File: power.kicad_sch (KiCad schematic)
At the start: 18 parts, among them IC1 STM32MP157AAB3

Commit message: Added Symbols
- MCP73830T
- STPMIC1BPQR
- MT41K256M16TW
- MCP73830
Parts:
- removed IC?: STPMIC1EPQR, QFN40P500X600X80-45N-D, symbol mp1lib:STPMIC1EPQR
- added IC2: STPMIC1BPQR, QFN40P500X600X80-45N-D, symbol ARMband:STPMIC1BPQR
- added IC3: STC3117IJT, BGA9C40P3X3_146X156X66, symbol ARMband:STC3117IJT
- added IC4: MCP73830T-2AAI_MYY, SON50P200X200X80-7N-D, symbol ARMband:MCP73830T-2AAI_MYY
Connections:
- net BUCK1IN: now also IC2.12 (BUCK2IN), IC2.24 (BUCK4IN), IC2.28 (BUCK3IN), IC2.8 (BUCK1IN)
- net BUCK_1V2: now also IC2.5 (VOUT1)
- net BUCK_1V8: now also IC2.31 (VOUT3)
- net BUCK_3V3: now also IC2.27 (VOUT4)
- net GND: now also IC2.10 (PGND2), IC2.26 (PGND4), IC2.30 (PGND3), IC2.6 (PGND1)
- net LDO1_1V8: now also IC2.23 (LDO1OUT)
- net VDD_DDR: now also IC2.9 (VOUT2)
- net VLX1: now also IC2.7 (VLX1)
- net VLX2: now also IC2.11 (VLX2)
- net VLX3: now also IC2.29 (VLX3)
- net VLX4: now also IC2.25 (VLX4)
- net VREF_DDR: now also IC2.16 (VREFDDR)
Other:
- note removed: "TODO: remake symbol + add to library! ;("
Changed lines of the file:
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@@
     (effects (font (size 1.27 1.27)) (justify left bottom))
-  )
-  (text "TODO: remake symbol + add to library! ;(" (at 57.15 123.19 0)
-    (effects (font (face "Yu Gothic UI") (size 2.54 2.54) (thickness 0.508) bold (color 255 0 6 1)) (justify left bottom))
   )
   (text "A:\n3V3 500mA @ HP mode\n	50 - 200 mA @ LP mode\nB:\n1V8 500mA @ HP mode\n	50 - 200 mA @ LP mode"
@@
         (path "/017c50c6-333c-4d31-ad5a-278994a09b14/5731d22b-18c2-4920-9f80-2a6ce209edf2"
           (reference "#PWR?") (unit 1)
+        )
+      )
+    )
+  )
+  (symbol (lib_id "ARMband:STPMIC1BPQR") (at 67.31 49.53 0) (unit 1)
+    (in_bom yes) (on_board yes) (dnp no) (fields_autoplaced)
+    (property "Reference" "IC2" (at 99.7459 94.3817 0)
+      (effects (font (size 1.27 1.27)) (justify left))
+    )
+    (property "Value" "STPMIC1BPQR" (at 99.7459 96.3027 0)
+      (effects (font (size 1.27 1.27)) (justify left))
+    )
+    (property "Footprint" "QFN40P500X600X80-45N-D" (at 104.14 34.29 0)
+      (effects (font (size 1.27 1.27)) (justify left) hide)
+    )
+    (property "Datasheet" "" (at 104.14 36.83 0)
+      (effects (font (size 1.27 1.27)) (justify left) hide)
+    )
+    (property "Description" "Power Management Specialized - PMIC" (at 104.14 39.37 0)
+      (effects (font (size 1.27 1.27)) (justify left) hide)
+    )
+    (property "Height" "0.8" (at 104.14 41.91 0)
+      (effects (font (size 1.27 1.27)) (justify left) hide)
+    )
+    (property "Mouser Part Number" "511-STPMIC1BPQR" (at 104.14 44.45 0)
+      (effects (font (size 1.27 1.27)) (justify left) hide)
+    )
+    (property "Mouser Price/Stock" "https://www.mouser.co.uk/ProductDetail/STMicroelectronics/STPMIC1BPQR?qs=%252B6g0mu59x7I4ukJ6TbOLhg%3D%3D" (at 104.14 46.99 0)
+      (effects (font (size 1.27 1.27)) (justify left) hide)
+    )
+    (property "Manufacturer_Name" "STMicroelectronics" (at 104.14 49.53 0)
+      (effects (font (size 1.27 1.27)) (justify left) hide)
+    )
+    (property "Manufacturer_Part_Number" "STPMIC1BPQR" (at 104.14 52.07 0)
+      (effects (font (size 1.27 1.27)) (justify left) hide)
+    )
+    (pin "1")
+    (pin "10")
+    (pin "11")
+    (pin "12")
+    (pin "13")
+    (pin "14")
+    (pin "15")
+    (pin "16")
+    (pin "17")
+    (pin "18")
+    (pin "19")
+    (pin "2")
+    (pin "20")
+    (pin "21")
+    (pin "22")
+    (pin "23")
+    (pin "24")
+    (pin "25")
+    (pin "26")
+    (pin "27")
+    (pin "28")
+    (pin "29")
+    (pin "3")
+    (pin "30")
+    (pin "31")
+    (pin "32")
+    (pin "33")
+    (pin "34")
+    (pin "35")
+    (pin "36")
+    (pin "37")
+    (pin "38")
+    (pin "39")
+    (pin "4")
+    (pin "40")
+    (pin "41")
+    (pin "42")
+    (pin "43")
+    (pin "44")
+    (pin "45")
+    (pin "5")
+    (pin "6")
+    (pin "7")
+    (pin "8")
+    (pin "9")
+    (instances
+      (project "gba"
+        (path "/017c50c6-333c-4d31-ad5a-278994a09b14/5731d22b-18c2-4920-9f80-2a6ce209edf2"
+          (reference "IC2") (unit 1)
         )
       )
@@
     )
   )
+  (symbol (lib_id "ARMband:STC3117IJT") (at 25.4 120.65 0) (unit 1)
+    (in_bom yes) (on_board yes) (dnp no) (fields_autoplaced)
+    (property "Reference" "IC3" (at 39.37 115.1509 0)
+      (effects (font (size 1.27 1.27)))
+    )
+    (property "Value" "STC3117IJT" (at 39.37 117.0719 0)
+      (effects (font (size 1.27 1.27)))
+    )
+    (property "Footprint" "BGA9C40P3X3_146X156X66" (at 49.53 118.11 0)
+      (effects (font (size 1.27 1.27)) (justify left) hide)
+    )
+    (property "Datasheet" "http://www.st.com/content/ccc/resource/technical/document/datasheet/ea/b5/01/6e/dd/f0/49/3e/DM00105047.pdf/files/DM00105047.pdf/jcr:content/translations/en.DM00105047.pdf" (at 49.53 120.65 0)
+      (effects (font (size 1.27 1.27)) (justify left) hide)
+    )
+    (property "Description" "Battery Management ANALOG" (at 49.53 123.19 0)
+      (effects (font (size 1.27 1.27)) (justify left) hide)
+    )
+    (property "Height" "0.655" (at 49.53 125.73 0)
+      (effects (font (size 1.27 1.27)) (justify left) hide)
+    )
+    (property "Mouser Part Number" "511-STC3117IJT" (at 49.53 128.27 0)
+      (effects (font (size 1.27 1.27)) (justify left) hide)
+    )
+    (property "Mouser Price/Stock" "https://www.mouser.co.uk/ProductDetail/STMicroelectronics/STC3117IJT?qs=JkuGhO7zlpmFAm2OGW2bCw%3D%3D" (at 49.53 130.81 0)
+      (effects (font (size 1.27 1.27)) (justify left) hide)
+    )
+    (property "Manufacturer_Name" "STMicroelectronics" (at 49.53 133.35 0)
+      (effects (font (size 1.27 1.27)) (justify left) hide)
+    )
+    (property "Manufacturer_Part_Number" "STC3117IJT" (at 49.53 135.89 0)
+      (effects (font (size 1.27 1.27)) (justify left) hide)
+    )
+    (pin "A1")
+    (pin "A2")
+    (pin "A3")
+    (pin "B1")
+    (pin "B2")
+    (pin "B3")
+    (pin "C1")
+    (pin "C2")
+    (pin "C3")
+    (instances
+      (project "gba"
+        (path "/017c50c6-333c-4d31-ad5a-278994a09b14/5731d22b-18c2-4920-9f80-2a6ce209edf2"
+          (reference "IC3") (unit 1)
+        )
+      )
+    )
+  )
   (symbol (lib_id "Device:L_Small") (at 238.76 52.07 90) (unit 1)
     (in_bom yes) (on_board yes) (dnp no) (fields_autoplaced)
@@
         (path "/017c50c6-333c-4d31-ad5a-278994a09b14/5731d22b-18c2-4920-9f80-2a6ce209edf2"
           (reference "#PWR?") (unit 1)
-        )
-      )
-    )
-  )
-  (symbol (lib_id "mp1lib:STPMIC1EPQR") (at 67.31 49.53 0) (unit 1)
-    (in_bom yes) (on_board yes) (dnp no) (fields_autoplaced)
-    (property "Reference" "IC?" (at 99.8094 94.8087 0)
-      (effects (font (size 1.27 1.27)) (justify left))
-    )
-    (property "Value" "STPMIC1EPQR" (at 99.8094 97.5838 0)
-      (effects (font (size 1.27 1.27)) (justify left))
-    )
-    (property "Footprint" "QFN40P500X600X80-45N-D" (at 104.14 34.29 0)
-      (effects (font (size 1.27 1.27)) (justify left) hide)
-    )
-    (property "Datasheet" "https://www.arrow.com/en/products/stpmic1epqr/stmicroelectronics" (at 104.14 36.83 0)
-      (effects (font (size 1.27 1.27)) (justify left) hide)
-    )
-    (property "Description" "Power Management Specialised - PMIC 14 Output Rails PMIC 4 Adjustable (COT) Buck SMPS converters BOOST with Bypass" (at 104.14 39.37 0)
-      (effects (font (size 1.27 1.27)) (justify left) hide)
-    )
-    (property "Height" "0.8" (at 104.14 41.91 0)
-      (effects (font (size 1.27 1.27)) (justify left) hide)
-    )
-    (property "Mouser Part Number" "511-STPMIC1EPQR" (at 104.14 44.45 0)
-      (effects (font (size 1.27 1.27)) (justify left) hide)
-    )
-    (property "Mouser Price/Stock" "https://www.mouser.co.uk/ProductDetail/STMicroelectronics/STPMIC1EPQR?qs=DPoM0jnrROUEouVjetqkFQ%3D%3D" (at 104.14 46.99 0)
-      (effects (font (size 1.27 1.27)) (justify left) hide)
-    )
-    (property "Manufacturer_Name" "STMicroelectronics" (at 104.14 49.53 0)
-      (effects (font (size 1.27 1.27)) (justify left) hide)
-    )
-    (property "Manufacturer_Part_Number" "STPMIC1EPQR" (at 104.14 52.07 0)
-      (effects (font (size 1.27 1.27)) (justify left) hide)
-    )
-    (pin "1")
-    (pin "10")
-    (pin "11")
-    (pin "12")
-    (pin "13")
-    (pin "14")
-    (pin "15")
-    (pin "16")
-    (pin "17")
-    (pin "18")
-    (pin "19")
-    (pin "2")
-    (pin "20")
-    (pin "21")
-    (pin "22")
-    (pin "23")
-    (pin "24")
-    (pin "25")
-    (pin "26")
-    (pin "27")
-    (pin "28")
-    (pin "29")
-    (pin "3")
-    (pin "30")
-    (pin "31")
-    (pin "32")
-    (pin "33")
-    (pin "34")
-    (pin "35")
-    (pin "36")
-    (pin "37")
-    (pin "38")
-    (pin "39")
-    (pin "4")
-    (pin "40")
-    (pin "41")
-    (pin "42")
-    (pin "43")
-    (pin "44")
-    (pin "45")
-    (pin "5")
-    (pin "6")
-    (pin "7")
-    (pin "8")
-    (pin "9")
-    (instances
-      (project "gba"
-        (path "/017c50c6-333c-4d31-ad5a-278994a09b14/5731d22b-18c2-4920-9f80-2a6ce209edf2"
-          (reference "IC?") (unit 1)
         )
       )
@@
         )
       )
+    )
+  )
+  (symbol (lib_id "ARMband:MCP73830T-2AAI_MYY") (at 24.13 151.13 0) (unit 1)
+    (in_bom yes) (on_board yes) (dnp no) (fields_autoplaced)
+    (property "Reference" "IC4" (at 39.37 145.6309 0)
+      (effects (font (size 1.27 1.27)))
+    )
+    (property "Value" "MCP73830T-2AAI_MYY" (at 39.37 147.5519 0)
+      (effects (font (size 1.27 1.27)))
+    )
+    (property "Footprint" "SON50P200X200X80-7N-D" (at 50.8 148.59 0)
+      (effects (font (size 1.27 1.27)) (justify left) hide)
+    )
+    (property "Datasheet" "http://www.microchip.com/mymicrochip/filehandler.aspx?ddocname=en555820" (at 50.8 151.13 0)
+      (effects (font (size 1.27 1.27)) (justify left) hide)
+    )
+    (property "Description" "Battery Management 1A LI-ION BATTERY CHARGE MGNT CNTRLR" (at 50.8 153.67 0)
+      (effects (font (size 1.27 1.27)) (justify left) hide)
+    )
+    (property "Height" "0.8" (at 50.8 156.21 0)
+      (effects (font (size 1.27 1.27)) (justify left) hide)
+    )
+    (property "Mouser Part Number" "579-MCP73830T2AAIMYY" (at 50.8 158.75 0)
+      (effects (font (size 1.27 1.27)) (justify left) hide)
+    )
+    (property "Mouser Price/Stock" "https://www.mouser.co.uk/ProductDetail/Microchip-Technology-Atmel/MCP73830T-2AAI-MYY?qs=DfG0HhEx1UUEr%2FUp7R8jlw%3D%3D" (at 50.8 161.29 0)
+      (effects (font (size 1.27 1.27)) (justify left) hide)
+    )
+    (property "Manufacturer_Name" "Microchip" (at 50.8 163.83 0)
+      (effects (font (size 1.27 1.27)) (justify left) hide)
+    )
+    (property "Manufacturer_Part_Number" "MCP73830T-2AAI/MYY" (at 50.8 166.37 0)
+      (effects (font (size 1.27 1.27)) (justify left) hide)
+    )
+    (pin "1")
+    (pin "2")
+    (pin "3")
+    (pin "4")
+    (pin "5")
+    (pin "6")
+    (pin "7")
+    (instances
+      (project "gba"
+        (path "/017c50c6-333c-4d31-ad5a-278994a09b14/5731d22b-18c2-4920-9f80-2a6ce209edf2"
+          (reference "IC4") (unit 1)
+        )
+      )

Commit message: Updated Symbols + Added Supply connections
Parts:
- removed C? (x4): 22uF, symbol Device:C_Small
- removed C? (x4): 10uF, symbol Device:C_Small
- removed IC2: STPMIC1BPQR, QFN40P500X600X80-45N-D, symbol ARMband:STPMIC1BPQR
- removed L? (x4): 1uH, symbol Device:L_Small
- removed R? (x4): 0R, symbol Device:R_Small
- added C10, C11, C12, C13, C14, C15, C16, C17, C18, C19, C20, C21, C22, C23, C24, C25, C26, C3, C4, C5, C6, C7, C8, C9: C_Small, symbol Device:C_Small
- added IC5: MT41K256M16TW-107_P, ARMband:BGA96C80P9X16_800X1400X120, symbol ARMband:MT41K256M16TW-107_P
- added IC6: STPMIC1BPQR, ARMband:QFN40P500X600X80-45N-D, symbol ARMband:STPMIC1BPQR
- added L1, L2, L3, L4, L5: L_Small, symbol Device:L_Small
- added R6, R7: R_Small, symbol Device:R_Small
- IC3: footprint BGA9C40P3X3_146X156X66 -> ARMband:BGA9C40P3X3_146X156X66
- IC4: footprint SON50P200X200X80-7N-D -> ARMband:SON50P200X200X80-7N-D
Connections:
- net BUCK_1V2: now also C7.2, IC6.5 (VOUT1), L1.2
- net BUCK_1V8: now also C9.2, IC6.31 (VOUT3), L3.2
- net BUCK_3V3: now also C10.2, IC6.27 (VOUT4), IC6.42 (VIO), L4.2, R6.1, R7.2; no longer IC1.W12 (VDD3V3_USBHS), IC1.W15 (VDD3V3_USBFS)
- net GND: now also IC3.A3 (GND), IC4.1 (VSS), IC4.7 (EP), C10.1, C11.1, C12.1, C13.1, C14.1, C15.1, C16.1, C17.1, C18.1, C19.1, C20.1, C21.1, C22.1, C23.1, C24.1, C25.1, C26.1, C3.1, C4.1, C5.1, C6.1, C7.1, C8.1, C9.1, IC5.A9 (VSS_1), IC5.B1 (VSSQ_1), IC5.B3 (VSS_2), IC5.B9 (VSSQ_2), IC5.D1 (VSSQ_3), IC5.D8 (VSSQ_4), IC5.E1 (VSS_3), IC5.E2 (VSSQ_5), IC5.E8 (VSSQ_6), IC5.F9 (VSSQ_7), IC5.G1 (VSSQ_8), IC5.G8 (VSS_4), IC5.G9 (VSSQ_9), IC5.J2 (VSS_5), IC5.J8 (VSS_6), IC5.M1 (VSS_7), IC5.M9 (VSS_8), IC5.P1 (VSS_9), IC5.P9 (VSS_10), IC5.T1 (VSS_11), IC5.T9 (VSS_12), IC6.10 (PGND2), IC6.15 (GNDLDO), IC6.26 (PGND4), IC6.30 (PGND3), IC6.41 (AGND), IC6.45 (EPGND), IC6.6 (PGND1)
- net VDD_DDR: now also C24.2, C8.2, IC5.A1 (VDDQ_1), IC5.A8 (VDDQ_2), IC5.B2 (VDD_1), IC5.C1 (VDDQ_3), IC5.C9 (VDDQ_4), IC5.D2 (VDDQ_5), IC5.D9 (VDD_2), IC5.E9 (VDDQ_6), IC5.F1 (VDDQ_7), IC5.G7 (VDD_3), IC5.H2 (VDDQ_8), IC5.H9 (VDDQ_9), IC5.K2 (VDD_4), IC5.K8 (VDD_5), IC5.N1 (VDD_6), IC5.N9 (VDD_7), IC5.R1 (VDD_8), IC5.R9 (VDD_9), IC6.13 (LDO3IN), IC6.9 (VOUT2), L2.2
- net VREF_DDR: now also C17.2, IC5.H1 (VREFDQ), IC5.M8 (VREFCA), IC6.16 (VREFDDR)
- new net: IC6.29 (VLX3), L3.1
- new net: IC6.11 (VLX2), L2.1
- new net: C15.2, IC6.40 (INTLDO)
- new net: IC6.33 (VLXBST), L5.2
- new net: IC6.25 (VLX4), L4.1
- new net: IC6.3 (SDA), R7.1
- new net: IC6.4 (SCL), R6.2
- new net: IC6.7 (VLX1), L1.1
- new net BSTOUT: C11.2, IC6.34 (BOUT), IC6.37 (SWIN)
- new net VBUS_HOST: C13.2, IC6.38 (SWOUT)
- new net VBUS_OTG: C12.2, IC6.35 (VBUSOTG)
- new net VDD_USB: C14.2, IC1.W12 (VDD3V3_USBHS), IC1.W15 (VDD3V3_USBFS), IC6.39 (LDO4OUT)
- new net VIN: C22.2, C23.2, C25.2, C26.2, C3.2, C4.2, C5.2, C6.2, IC6.12 (BUCK2IN), IC6.19 (LDO25IN), IC6.22 (LDO16IN), IC6.24 (BUCK4IN), IC6.28 (BUCK3IN), IC6.36 (VIN), IC6.8 (BUCK1IN), L5.1
- new net VOUT_LDO1: C18.2, IC6.23 (LDO1OUT)
- new net VOUT_LDO2: C20.2, IC6.18 (LDO2OUT)
- new net VOUT_LDO5: C21.2, IC6.20 (LDO5OUT)
- new net VOUT_LDO6: C19.2, IC6.21 (LDO6OUT)
- new net VOUT_LOD3: C16.2, IC6.14 (LDO3OUT)
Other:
- note added: "1-1.5V 1000mA @ HP mode 50-200 @ LP mode 1.35V for our RAM!"
- note added: "? VBAT other uses"
- note added: "Battery Gas Gauge"
- note added: "DDR3L RAM Supply"
- note added: "Datasheet: P.11 VOUT_LDO3 = VREF_DDR = VOUT2/2?"
- note added: "Datasheet: P.49 VDD = nom. 1V35 VDDQ = nom. 1V35 VREFCA = 0.5 x VDD VREFDQ = 0.5 x VDD"
- note added: "Li-Ion Battery"
- note added: "Li-Ion Charging"
- note added: "Power Management"
- note added: "STM32 MP1 Supply"
- note added: "TODO"
- note added: "TODO: Is this fine? VOUT_LDO3 = VREF_DDR = VOUT2/2?"
- note added: "TODO: all GND connections together?"
- note added: "TODO: check for usable connections and connect!"
- note added: "connection to VDD -> this correct?"
- note removed: "1-1.5V 1000mA @ HP mode 50-200 @ LP mode"
- moved on the sheet: IC1B, IC4

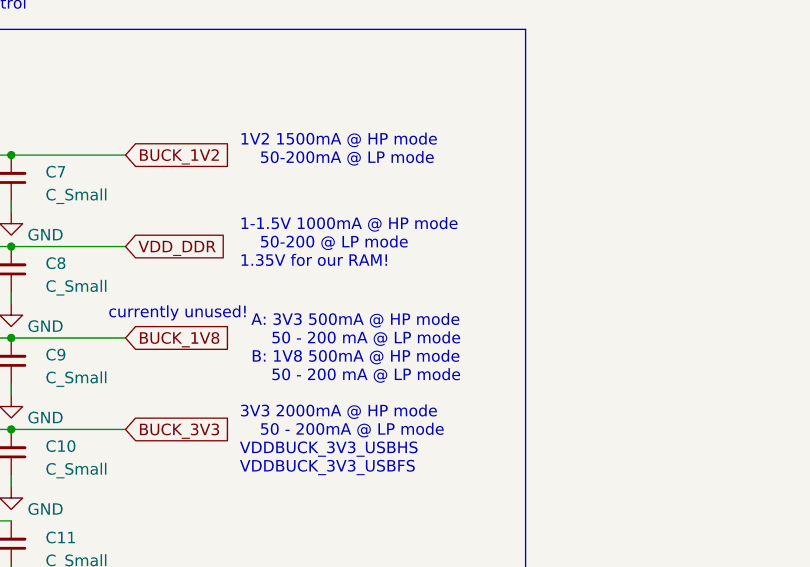
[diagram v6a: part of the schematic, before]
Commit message: Add comment regarding RAM voltage via software
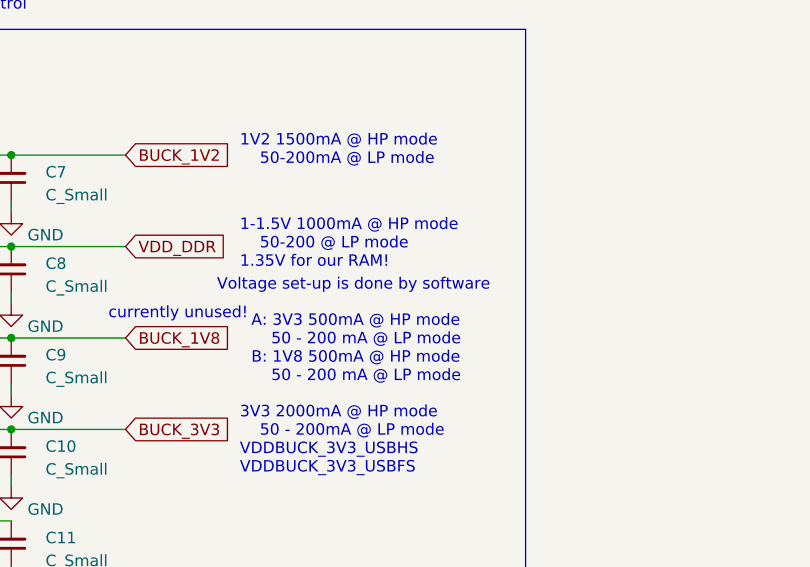
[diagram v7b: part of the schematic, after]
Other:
- note added: "Voltage set-up is done by software"
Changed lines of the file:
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@@
     (effects (font (size 1.27 1.27) (color 255 0 24 1)) (justify left bottom))
+  )
+  (text "Voltage set-up is done by software" (at 213.36 60.96 0)
+    (effects (font (size 1.27 1.27)) (justify left bottom))
   )
   (text "TODO: all GND connections together?" (at 393.065 351.79 0)
